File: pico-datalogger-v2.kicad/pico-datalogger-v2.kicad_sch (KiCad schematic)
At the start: 35 parts, among them J1 JST-PH2 Bat, J10 Conn_PCB_2, J11 Conn_I2C1, J12 Conn_UART_5V, J13 Conn_I2C1, J14 Conn_I2C0, J2 Conn_Pico_Left, J3 Conn_Pico_Right, J4 Alt-Bat, J5 Conn_LoRa, J6 Conn_Display, J7 Conn_PCB_1, J8 Conn_ADC, J9 Conn_I2C0, Q1 AO3401A, SW1 SW_ON, SW2 SW_RUN, U1 74LVC2G74, U2 PCF8523T, U3 Pico, U4 XTSD, Y1 Crystal

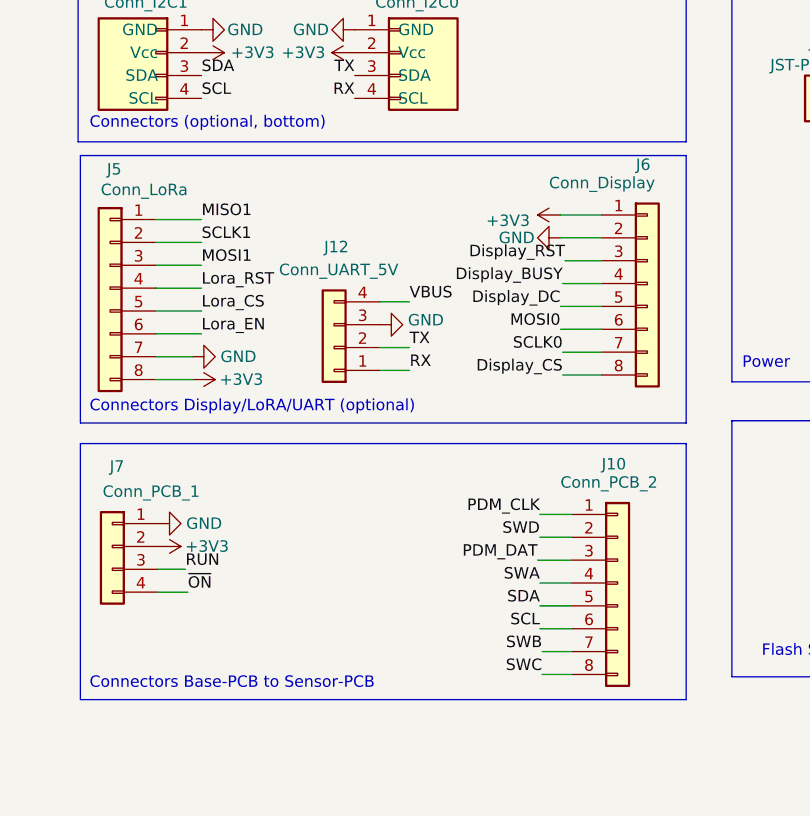
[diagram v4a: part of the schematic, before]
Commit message: make UART-5V compatible to Pimoroni PMS5003-adapter
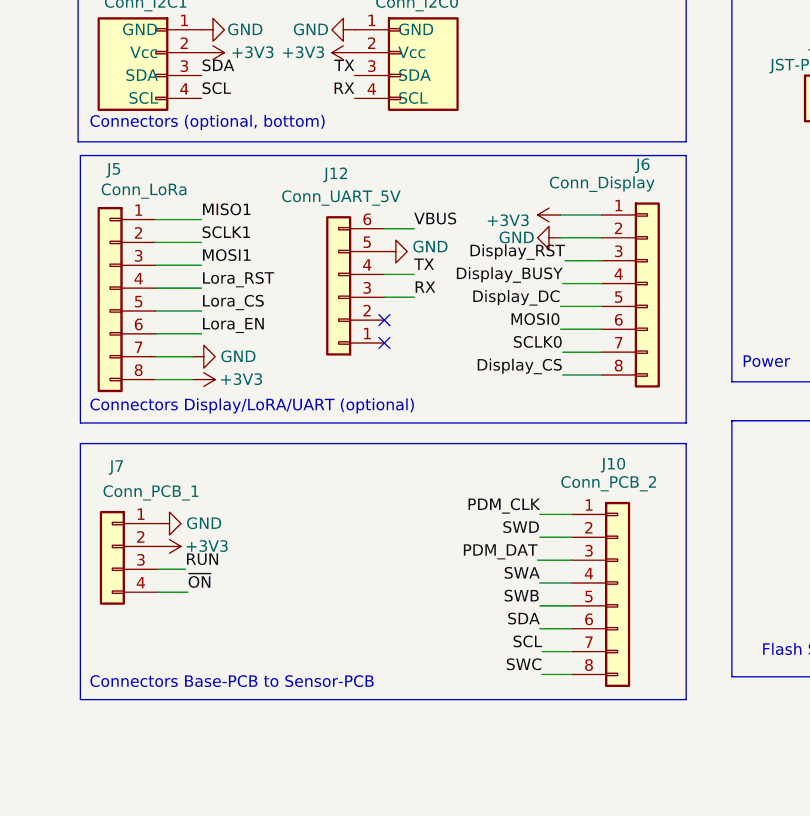
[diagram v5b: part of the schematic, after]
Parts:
- J12: footprint Connector_PinHeader_2.54mm:PinHeader_1x04_P2.54mm_Horizontal -> Connector_PinHeader_2.54mm:PinHeader_1x06_P2.54mm_Horizontal; symbol Connector_Generic:Conn_01x04 -> Connector_Generic:Conn_01x06
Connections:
- net GND: now also J12.5 (Pin_5); no longer J12.3 (Pin_3)
- net RX: now also J12.3 (Pin_3); no longer J12.1 (Pin_1)
- net SCL: now also J10.7 (Pin_7); no longer J10.6 (Pin_6)
- net SDA: now also J10.6 (Pin_6); no longer J10.5 (Pin_5)
- net SWB: now also J10.5 (Pin_5); no longer J10.7 (Pin_7)
- net TX: now also J12.4 (Pin_4); no longer J12.2 (Pin_2)
- net VBUS: now also J12.6 (Pin_6); no longer J12.4 (Pin_4)
- no-connect marks 8 -> 10
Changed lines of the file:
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@@
   (title_block
     (title "pico-datalogger-v2")
-    (date "2023-08-26")
-    (rev "0.92")
+    (date "2023-08-27")
+    (rev "0.93")
     (company "Bernhard Bablok")
     (comment 1 "https://github.com/bablokb/pcb-pico-datalogger")
@@
   (no_connect (at 76.708 82.042))
   (no_connect (at 91.948 41.402))
+  (no_connect (at 162.052 122.428))
   (no_connect (at 71.628 82.042))
   (no_connect (at 86.106 132.588))
   (no_connect (at 241.3 150.114))
+  (no_connect (at 162.052 119.888))
   (wire (pts (xy 143.51 39.37) (xy 144.78 39.37))
     (stroke (width 0) (type default) (color 0 0 0 0))
@@
     (stroke (width 0) (type default) (color 0 0 0 0))
   )
-  (wire (pts (xy 161.544 122.936) (xy 164.846 122.936))
+  (wire (pts (xy 162.052 114.808) (xy 165.354 114.808))
     (stroke (width 0) (type default) (color 0 0 0 0))
   )
@@
     (stroke (width 0) (type default) (color 0 0 0 0))
   )
-  (wire (pts (xy 161.544 117.856) (xy 164.846 117.856))
+  (wire (pts (xy 162.052 109.728) (xy 165.354 109.728))
     (stroke (width 0) (type default) (color 0 0 0 0))
   )
@@
     (stroke (width 0) (type default) (color 0 0 0 0))
   )
-  (wire (pts (xy 161.544 125.476) (xy 164.846 125.476))
+  (wire (pts (xy 162.052 117.348) (xy 165.354 117.348))
     (stroke (width 0) (type default) (color 0 0 0 0))
   )
@@
     (effects (font (size 1.27 1.27)) (justify left bottom))
   )
-  (label "TX" (at 164.846 122.936 0)
+  (label "TX" (at 165.354 114.808 0)
     (effects (font (size 1.27 1.27)) (justify left bottom))
   )
@@
     (effects (font (size 1.27 1.27)) (justify right bottom))
   )
-  (label "SWB" (at 179.578 156.718 180)
+  (label "SWB" (at 179.324 151.638 180)
     (effects (font (size 1.27 1.27)) (justify right bottom))
   )
@@
     (effects (font (size 1.27 1.27)) (justify left bottom))
   )
-  (label "RX" (at 164.846 125.476 0)
+  (label "RX" (at 165.354 117.348 0)
     (effects (font (size 1.27 1.27)) (justify left bottom))
   )
@@
     (effects (font (size 1.27 1.27)) (justify right bottom))
   )
-  (label "SCL" (at 179.324 154.178 180)
+  (label "SCL" (at 179.578 156.718 180)
     (effects (font (size 1.27 1.27)) (justify right bottom))
   )
@@
     (effects (font (size 1.27 1.27)) (justify right bottom))
   )
-  (label "VBUS" (at 164.846 117.856 0)
+  (label "VBUS" (at 165.354 109.728 0)
     (effects (font (size 1.27 1.27)) (justify left bottom))
   )
@@
     (effects (font (size 1.27 1.27)) (justify right bottom))
   )
-  (label "SDA" (at 179.324 151.638 180)
+  (label "SDA" (at 179.324 154.178 180)
     (effects (font (size 1.27 1.27)) (justify right bottom))
   )
@@
     (pin "1")
   )
-  (symbol (lib_id "power:GND") (at 161.544 120.396 90) (unit 1)
+  (symbol (lib_id "power:GND") (at 162.052 112.268 90) (unit 1)
     (in_bom yes) (on_board yes)
-    (property "Reference" "#PWR024" (id 0) (at 167.894 120.396 0)
+    (property "Reference" "#PWR024" (id 0) (at 168.402 112.268 0)
       (effects (font (size 1.27 1.27)) hide)
     )
-    (property "Value" "GND" (id 1) (at 168.656 119.888 90)
+    (property "Value" "GND" (id 1) (at 169.164 111.76 90)
       (effects (font (size 1.27 1.27)) (justify left))
     )
-    (property "Footprint" "" (id 2) (at 161.544 120.396 0)
+    (property "Footprint" "" (id 2) (at 162.052 112.268 0)
       (effects (font (size 1.27 1.27)) hide)
     )
-    (property "Datasheet" "" (id 3) (at 161.544 120.396 0)
+    (property "Datasheet" "" (id 3) (at 162.052 112.268 0)
       (effects (font (size 1.27 1.27)) hide)
     )
@@
     (pin "1")
   )
-  (symbol (lib_id "Connector_Generic:Conn_01x04") (at 156.464 122.936 180) (unit 1)
+  (symbol (lib_id "Connector_Generic:Conn_01x06") (at 156.972 117.348 180) (unit 1)
     (in_bom yes) (on_board yes)
-    (property "Reference" "J12" (id 0) (at 156.718 111.76 0))
-    (property "Value" "Conn_UART_5V" (id 1) (at 156.972 114.3 0))
-    (property "Footprint" "Connector_PinHeader_2.54mm:PinHeader_1x04_P2.54mm_Horizontal" (id 2) (at 156.464 122.936 0)
+    (property "Reference" "J12" (id 0) (at 156.718 103.632 0))
+    (property "Value" "Conn_UART_5V" (id 1) (at 157.226 106.172 0))
+    (property "Footprint" "Connector_PinHeader_2.54mm:PinHeader_1x06_P2.54mm_Horizontal" (id 2) (at 156.972 117.348 0)
       (effects (font (size 1.27 1.27)) hide)
     )
-    (property "Datasheet" "~" (id 3) (at 156.464 122.936 0)
+    (property "Datasheet" "~" (id 3) (at 156.972 117.348 0)
       (effects (font (size 1.27 1.27)) hide)
     )
@@
     (pin "3")
     (pin "4")
+    (pin "5")
+    (pin "6")
   )
   (symbol (lib_id "Connector_Generic:Conn_01x02") (at 210.058 93.98 0) (mirror y) (unit 1)
@@
     )
     (path "/f4141f83-f28d-484e-84bb-e85ebfe1aae8"
-      (reference "J12") (unit 1) (value "Conn_UART_5V") (footprint "Connector_PinHeader_2.54mm:PinHeader_1x04_P2.54mm_Horizontal")
+      (reference "J12") (unit 1) (value "Conn_UART_5V") (footprint "Connector_PinHeader_2.54mm:PinHeader_1x06_P2.54mm_Horizontal")
     )
     (path "/bc7549ff-6d62-42fe-97a5-86d96ed7fb61"

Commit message: added part-numbers
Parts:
- J10, J5, J6: LCSC (none) -> C5143489
- J11, J12, J13, J14, J9, SW1, SW2: now left out of the parts list
- J2, J3: LCSC C429947 -> C429947
- J7: LCSC (none) -> C495551
- JP1: now in the parts list
- Q1: LCSC C15127 -> C15127
- U1: LCSC C282355 -> C282355
- U2: LCSC C2651516 -> C2651516
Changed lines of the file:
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@@
   )
   (symbol (lib_id "Switch:SW_Push") (at 100.076 186.436 0) (unit 1)
-    (in_bom yes) (on_board yes)
+    (in_bom no) (on_board yes)
     (property "Reference" "SW2" (id 0) (at 100.33 178.816 0))
     (property "Value" "SW_RUN" (id 1) (at 100.076 181.61 0))
@@
   )
   (symbol (lib_id "user:Stemma-QT_Qwicc") (at 163.322 74.168 0) (unit 1)
-    (in_bom yes) (on_board yes)
+    (in_bom no) (on_board yes)
     (property "Reference" "J9" (id 0) (at 161.798 66.04 0)
       (effects (font (size 1.27 1.27)) (justify left))
@@
       (effects (font (size 1.27 1.27)) hide)
     )
-    (property "LCSC" "C429947 " (id 4) (at 62.738 142.748 0)
+    (property "LCSC" "C429947" (id 4) (at 62.738 142.748 0)
       (effects (font (size 1.27 1.27)) hide)
     )
@@
       (effects (font (size 1.27 1.27)) hide)
     )
+    (property "LCSC" "C5143489" (id 4) (at 191.262 115.824 0)
+      (effects (font (size 1.27 1.27)) hide)
+    )
     (pin "1")
     (pin "2")
@@
   )
   (symbol (lib_id "Switch:SW_Push") (at 215.646 71.12 0) (unit 1)
-    (in_bom yes) (on_board yes)
+    (in_bom no) (on_board yes)
     (property "Reference" "SW1" (id 0) (at 215.9 63.5 0))
     (property "Value" "SW_ON" (id 1) (at 215.646 66.294 0))
@@
       (effects (font (size 1.27 1.27)) hide)
     )
+    (property "LCSC" "C495551" (id 4) (at 131.826 145.034 0)
+      (effects (font (size 1.27 1.27)) hide)
+    )
     (pin "1")
     (pin "2")
@@
     )
     (property "Datasheet" "~" (id 3) (at 131.572 116.332 0)
+      (effects (font (size 1.27 1.27)) hide)
+    )
+    (property "LCSC" "C5143489" (id 4) (at 131.572 116.332 0)
       (effects (font (size 1.27 1.27)) hide)
     )
@@
       (effects (font (size 1.27 1.27)) hide)
     )
-    (property "LCSC" "C429947 " (id 4) (at 81.026 142.748 0)
+    (property "LCSC" "C429947" (id 4) (at 81.026 142.748 0)
       (effects (font (size 1.27 1.27)) hide)
     )
@@
   )
   (symbol (lib_id "user:Stemma-QT_Qwicc") (at 136.144 74.168 0) (mirror y) (unit 1)
-    (in_bom yes) (on_board yes)
+    (in_bom no) (on_board yes)
     (property "Reference" "J11" (id 0) (at 137.668 66.04 0)
       (effects (font (size 1.27 1.27)) (justify left))
@@
     )
     (property "Datasheet" "~" (id 3) (at 187.96 149.098 0)
+      (effects (font (size 1.27 1.27)) hide)
+    )
+    (property "LCSC" "C5143489" (id 4) (at 187.96 149.098 0)
       (effects (font (size 1.27 1.27)) hide)
     )
@@
       (effects (font (size 1.27 1.27)) (justify left) hide)
     )
-    (property "LCSC" "C15127 " (id 4) (at 255.778 115.57 0)
+    (property "LCSC" "C15127" (id 4) (at 255.778 115.57 0)
       (effects (font (size 1.27 1.27)) hide)
     )
@@
   )
   (symbol (lib_id "Jumper:Jumper_2_Bridged") (at 226.822 113.03 0) (unit 1)
-    (in_bom no) (on_board yes)
+    (in_bom yes) (on_board yes)
     (property "Reference" "JP1" (id 0) (at 226.822 107.95 0))
     (property "Value" "Jumper_VSYS" (id 1) (at 226.822 110.49 0))
@@
   )
   (symbol (lib_id "user:Stemma-QT_Qwicc") (at 136.652 90.17 0) (mirror y) (unit 1)
-    (in_bom yes) (on_board yes)
+    (in_bom no) (on_board yes)
     (property "Reference" "J13" (id 0) (at 135.89 82.55 0)
       (effects (font (size 1.27 1.27)) (justify left))
@@
       (effects (font (size 1.27 1.27)) hide)
     )
-    (property "LCSC" " C2651516 " (id 4) (at 166.37 44.45 0)
+    (property "LCSC" "C2651516" (id 4) (at 166.37 44.45 0)
       (effects (font (size 1.27 1.27)) hide)
     )
@@
   )
   (symbol (lib_id "Connector_Generic:Conn_01x06") (at 156.972 117.348 180) (unit 1)
-    (in_bom yes) (on_board yes)
+    (in_bom no) (on_board yes)
     (property "Reference" "J12" (id 0) (at 156.718 103.632 0))
     (property "Value" "Conn_UART_5V" (id 1) (at 157.226 106.172 0))
@@
       (effects (font (size 1.524 1.524)) (justify left) hide)
     )
-    (property "LCSC" "C282355 " (id 13) (at 251.46 50.038 0)
+    (property "LCSC" "C282355" (id 13) (at 251.46 50.038 0)
       (effects (font (size 1.27 1.27)) hide)
     )
@@
   )
   (symbol (lib_id "user:Stemma-QT_Qwicc") (at 163.83 90.17 0) (unit 1)
-    (in_bom yes) (on_board yes)
+    (in_bom no) (on_board yes)
     (property "Reference" "J14" (id 0) (at 165.1 82.804 0)
       (effects (font (size 1.27 1.27)) (justify left))

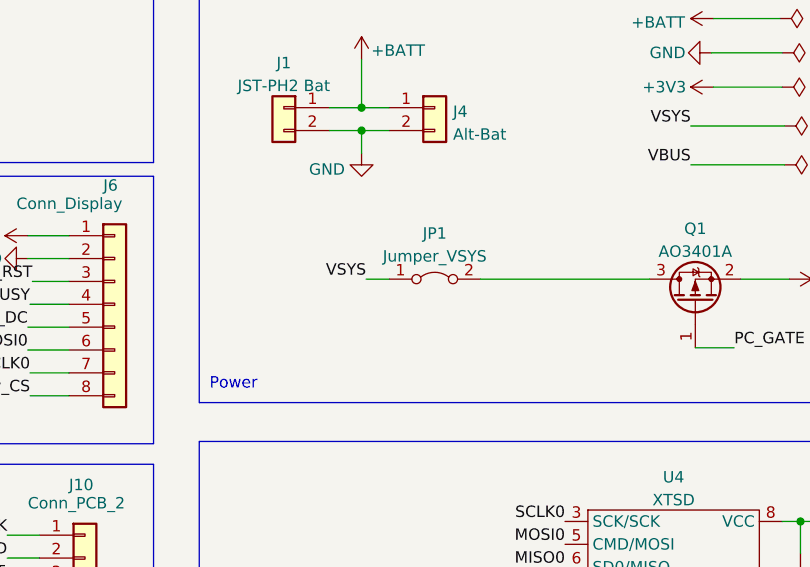
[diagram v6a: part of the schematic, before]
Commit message: Rev 0.94: use mosfet instead of jumper for VSYS
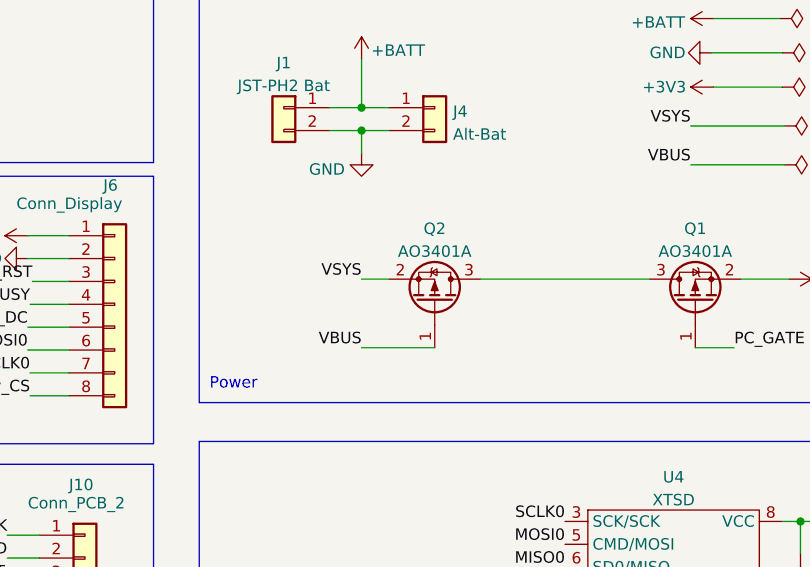
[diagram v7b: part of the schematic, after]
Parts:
- removed JP1: Jumper_VSYS, Connector_PinHeader_2.54mm:PinHeader_1x02_P2.54mm_Vertical, symbol Jumper:Jumper_2_Bridged
- added Q2: AO3401A, Package_TO_SOT_SMD:SOT-23, symbol Transistor_FET:AO3401A
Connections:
- net VBUS: now also Q2.1 (G)
- net VSYS: now also Q2.2 (S)
- net at Q1.3 (D): now also Q2.3 (D)
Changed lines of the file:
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@@
   (title_block
     (title "pico-datalogger-v2")
-    (date "2023-08-27")
-    (rev "0.93")
+    (date "2023-11-25")
+    (rev "0.94")
     (company "Bernhard Bablok")
     (comment 1 "https://github.com/bablokb/pcb-pico-datalogger")
@@
     (stroke (width 0) (type default) (color 0 0 0 0))
   )
+  (wire (pts (xy 218.694 120.65) (xy 226.822 120.65))
+    (stroke (width 0) (type default) (color 0 0 0 0))
+  )
   (wire (pts (xy 157.48 25.4) (xy 157.48 34.29))
     (stroke (width 0) (type default) (color 0 0 0 0))
@@
     (stroke (width 0) (type default) (color 0 0 0 0))
   )
-  (wire (pts (xy 219.202 113.03) (xy 221.742 113.03))
-    (stroke (width 0) (type default) (color 0 0 0 0))
-  )
   (wire (pts (xy 236.982 41.148) (xy 242.57 41.148))
     (stroke (width 0) (type default) (color 0 0 0 0))
@@
     (stroke (width 0) (type default) (color 0 0 0 0))
   )
+  (wire (pts (xy 218.694 113.03) (xy 221.742 113.03))
+    (stroke (width 0) (type default) (color 0 0 0 0))
+  )
   (wire (pts (xy 175.26 34.29) (xy 175.26 26.035))
     (stroke (width 0) (type default) (color 0 0 0 0))
@@
     (effects (font (size 1.27 1.27)) (justify left bottom))
   )
+  (label "VBUS" (at 218.694 120.65 180)
+    (effects (font (size 1.27 1.27)) (justify right bottom))
+  )
   (label "SCLK1" (at 141.732 111.252 0)
     (effects (font (size 1.27 1.27)) (justify left bottom))
@@
     (effects (font (size 1.27 1.27)) (justify left bottom))
   )
-  (label "VSYS" (at 219.202 113.03 180)
-    (effects (font (size 1.27 1.27)) (justify right bottom))
-  )
   (label "~{ON}" (at 140.208 150.114 0)
     (effects (font (size 1.27 1.27)) (justify left bottom))
@@
     (effects (font (size 1.27 1.27)) (justify left bottom))
   )
+  (label "VSYS" (at 218.694 113.03 180)
+    (effects (font (size 1.27 1.27)) (justify right bottom))
+  )
   (label "Display_BUSY" (at 181.864 115.824 180)
     (effects (font (size 1.27 1.27)) (justify right bottom))
@@
     (pin "1")
   )
-  (symbol (lib_id "Jumper:Jumper_2_Bridged") (at 226.822 113.03 0) (unit 1)
-    (in_bom yes) (on_board yes)
-    (property "Reference" "JP1" (id 0) (at 226.822 107.95 0))
-    (property "Value" "Jumper_VSYS" (id 1) (at 226.822 110.49 0))
-    (property "Footprint" "Connector_PinHeader_2.54mm:PinHeader_1x02_P2.54mm_Vertical" (id 2) (at 226.822 113.03 0)
-      (effects (font (size 1.27 1.27)) hide)
-    )
-    (property "Datasheet" "~" (id 3) (at 226.822 113.03 0)
-      (effects (font (size 1.27 1.27)) hide)
-    )
-    (pin "1")
-    (pin "2")
-  )
   (symbol (lib_id "power:GND") (at 181.61 110.744 270) (unit 1)
     (in_bom yes) (on_board yes)
@@
     (pin "1")
   )
+  (symbol (lib_id "Transistor_FET:AO3401A") (at 226.822 115.57 270) (mirror x) (unit 1)
+    (in_bom yes) (on_board yes) (fields_autoplaced)
+    (property "Reference" "Q2" (id 0) (at 226.822 107.4252 90))
+    (property "Value" "AO3401A" (id 1) (at 226.822 109.9621 90))
+    (property "Footprint" "Package_TO_SOT_SMD:SOT-23" (id 2) (at 224.917 110.49 0)
+      (effects (font (size 1.27 1.27) italic) (justify left) hide)
+    )
+    (property "Datasheet" "http://www.aosmd.com/pdfs/datasheet/AO3401A.pdf" (id 3) (at 226.822 115.57 0)
+      (effects (font (size 1.27 1.27)) (justify left) hide)
+    )
+    (property "LCSC" "C15127" (id 4) (at 226.822 115.57 0)
+      (effects (font (size 1.27 1.27)) hide)
+    )
+    (pin "1")
+    (pin "2")
+    (pin "3")
+  )
   (symbol (lib_id "Device:R_Small") (at 265.176 45.212 180) (unit 1)
     (in_bom yes) (on_board yes)
@@
       (reference "J14") (unit 1) (value "Conn_I2C0") (footprint "Connector_PinHeader_2.54mm:PinHeader_1x04_P2.54mm_Vertical")
     )
-    (path "/a2bbecfe-02e1-46bb-a8e7-6ba53ada3091"
-      (reference "JP1") (unit 1) (value "Jumper_VSYS") (footprint "Connector_PinHeader_2.54mm:PinHeader_1x02_P2.54mm_Vertical")
-    )
     (path "/9ac2cb99-c8db-4b2c-88eb-57c67491b260"
       (reference "Q1") (unit 1) (value "AO3401A") (footprint "Package_TO_SOT_SMD:SOT-23")
     )
+    (path "/d362b9c4-1583-47cc-8668-e43dbe4c326a"
+      (reference "Q2") (unit 1) (value "AO3401A") (footprint "Package_TO_SOT_SMD:SOT-23")
+    )
     (path "/d5218d0f-acc5-4d6b-8356-4954b7c791e8"

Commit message: added THT-connectors, finished routing
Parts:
- removed J4: Alt-Bat, Connector_PinHeader_2.54mm:PinHeader_1x02_P2.54mm_Vertical, symbol Connector_Generic:Conn_01x02
- removed J7: Conn_PCB_1, Connector_JST:JST_SUR_BM04B-SURS-TF_1x04-1MP_P0.80mm_Vertical, symbol Connector_Generic:Conn_01x04
- added J15: PCB_2_THT, Connector_PinHeader_2.54mm:PinHeader_1x08_P2.54mm_Vertical, symbol Connector_Generic:Conn_01x08
- added J16: LoRa_THT, Connector_PinHeader_2.54mm:PinHeader_1x08_P2.54mm_Vertical, symbol Connector_Generic:Conn_01x08
- added J17: Disp_THT, Connector_PinHeader_2.54mm:PinHeader_1x08_P2.54mm_Vertical, symbol Connector_Generic:Conn_01x08
- added J4: PCB_1_THT, Connector_PinHeader_2.54mm:PinHeader_1x04_P2.54mm_Vertical, symbol Connector_Generic:Conn_01x04
- added J7: Conn_PCB_1, Connector_JST:JST_SUR_BM08B-SURS-TF_1x08-1MP_P0.80mm_Vertical, symbol Connector_Generic:Conn_01x08
- added R5, R7: 10K, Resistor_SMD:R_0402_1005Metric, symbol Device:R_Small
- added R6: 100K, Resistor_SMD:R_0402_1005Metric, symbol Device:R_Small
- SW1: symbol Switch:SW_Push -> user:SW_Push_Vertical; now in the parts list
- SW2: value SW_RUN -> SW_RST; symbol Switch:SW_Push -> user:SW_Push_Vertical; now in the parts list
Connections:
- net +3V3: now also J16.8 (Pin_8), J17.1 (Pin_1), J4.2 (Pin_2), J7.3 (Pin_3), J7.4 (Pin_4), R5.1, R7.1
- net Display_BUSY: now also J17.4 (Pin_4)
- net Display_CS: now also J17.8 (Pin_8), R5.2
- net Display_DC: now also J17.5 (Pin_5)
- net Display_RST: now also J17.3 (Pin_3)
- net GND: now also J16.7 (Pin_7), J17.2 (Pin_2), J4.1 (Pin_1), J7.1 (Pin_1), J7.2 (Pin_2), R6.2
- net Lora_CS: now also J16.5 (Pin_5)
- net Lora_EN: now also J16.6 (Pin_6)
- net Lora_RST: now also J16.4 (Pin_4)
- net MISO0: now also R6.1
- net MISO1: now also J16.1 (Pin_1)
- net MOSI0: now also J17.6 (Pin_6)
- net MOSI1: now also J16.3 (Pin_3)
- net PDM_CLK: now also J15.1 (Pin_1)
- net PDM_DAT: now also J15.3 (Pin_3)
- net RUN: now also J4.3 (Pin_3), J7.7 (Pin_7)
- net SCL: now also J15.7 (Pin_7)
- net SCLK0: now also J17.7 (Pin_7)
- net SCLK1: now also J16.2 (Pin_2)
- net SDA: now also J15.6 (Pin_6)
- net SD_CS: now also R7.2
- net SWA: now also J15.4 (Pin_4)
- net SWB: now also J15.5 (Pin_5)
- net SWC: now also J15.8 (Pin_8)
- net SWD: now also J15.2 (Pin_2)
- net ~{ON}: now also J4.4 (Pin_4), J7.8 (Pin_8)
- no-connect marks 10 -> 12
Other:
- moved on the sheet: J10, J11, J12, J13, J14, J6, J8, J9
